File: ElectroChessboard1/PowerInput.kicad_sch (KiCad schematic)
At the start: 8 parts, among them J1 USB_B

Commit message: Added but not connected yet SD Card pins and RTC
.
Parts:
- J1: footprint (none) -> Connector_USB:USB_B_Lumberg_2411_02_Horizontal
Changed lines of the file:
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@@
 			)
 		)
-		(property "Footprint" ""
+		(property "Footprint" "Connector_USB:USB_B_Lumberg_2411_02_Horizontal"
 			(at 48.26 45.72 0)
 			(effects

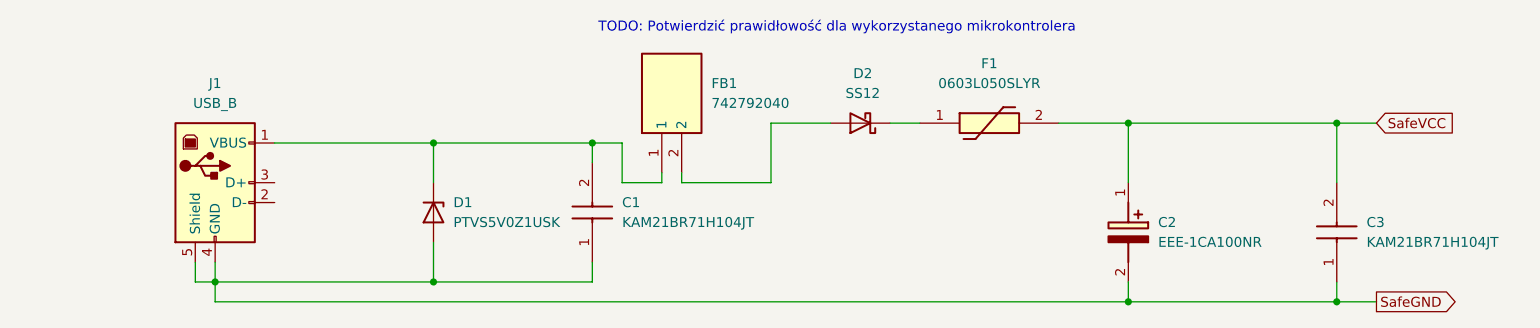
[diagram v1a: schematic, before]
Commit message: Corrected footprints 1
Chosen footprints for JLCPCB
I may add USB insterface chip
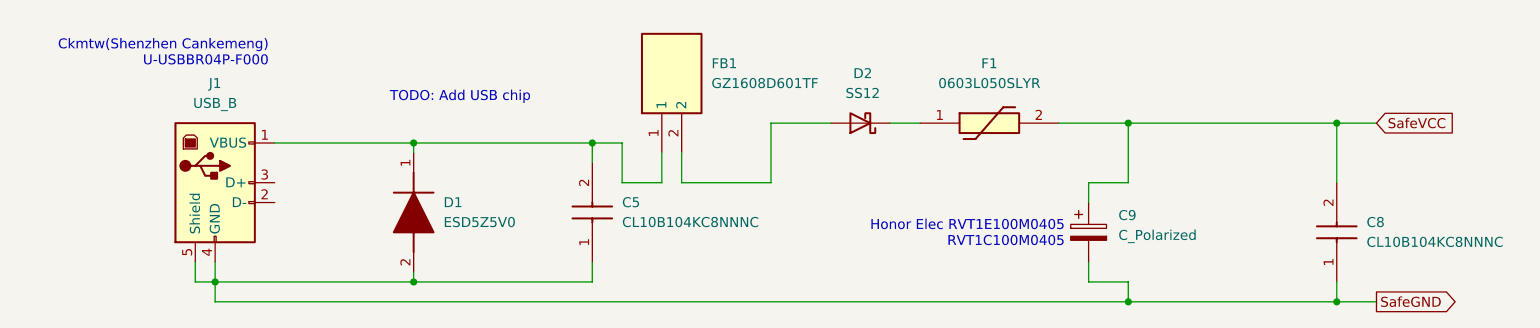
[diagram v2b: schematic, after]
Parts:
- removed C1, C3: KAM21BR71H104JT, CAPC2012X94N, symbol SamacSys_Parts:KAM21BR71H104JT
- removed C2: EEE-1CA100NR, EEE0GA101SR, symbol SamacSys_Parts:EEE-1CA100NR
- removed D1: PTVS5V0Z1USK, Diode_SMD:Nexperia_DSN1608-2_1.6x0.8mm, symbol Diode:PTVS5V0Z1USK
- removed FB1: 742792040, BEADC2012X110N, symbol SamacSys_Parts:742792040
- added C5, C8: CL10B104KC8NNNC, SamacSys_Parts:CAPC1608X90N, symbol SamacSys_Parts:CL10B104KC8NNNC
- added C9: C_Polarized, Capacitor_SMD:CP_Elec_4x5.4, symbol Device:C_Polarized
- added D1: ESD5Z5V0, SODFL1608X70N, symbol SamacSys_Parts:ESD5Z5V0
- added FB1: GZ1608D601TF, BEADC1608X95N, symbol SamacSys_Parts:GZ1608D601TF
- F1: footprint 0603L050SLYR -> SamacSys_Parts:0603L050SLYR
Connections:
- net SafeGND: now also C5.1, C8.1, C9.2, D1.2 (A)
- net SafeVCC: now also C8.2, C9.1
- net at J1.1 (VBUS): now also C5.2, D1.1 (K), FB1.1
- net at D2.2 (A): now also FB1.2
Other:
- note added: "Ckmtw(Shenzhen Cankemeng) U-USBBR04P-F000"
- note added: "Honor Elec RVT1E100M0405 RVT1C100M0405"
- note added: "TODO: Add USB chip"
- note removed: "TODO: Potwierdzić prawidłowość dla wykorzystanego mikrokontrolera"

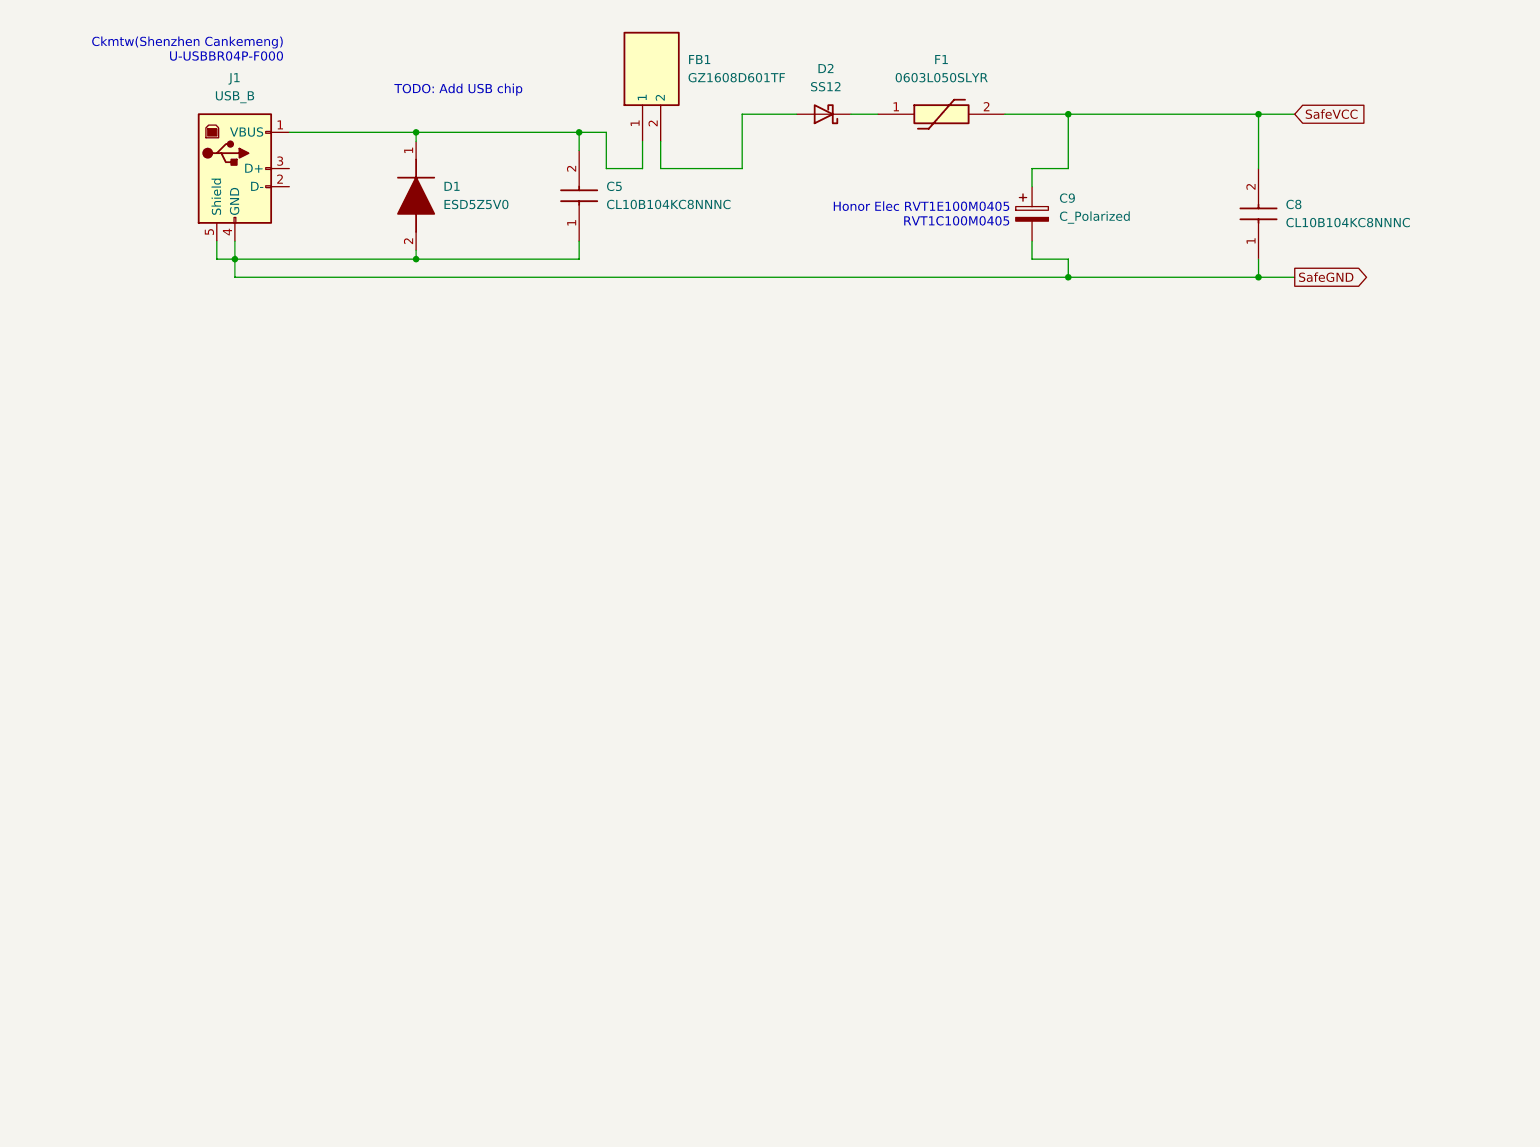
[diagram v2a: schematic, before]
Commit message: Added FT232RL
Ready for PCB design
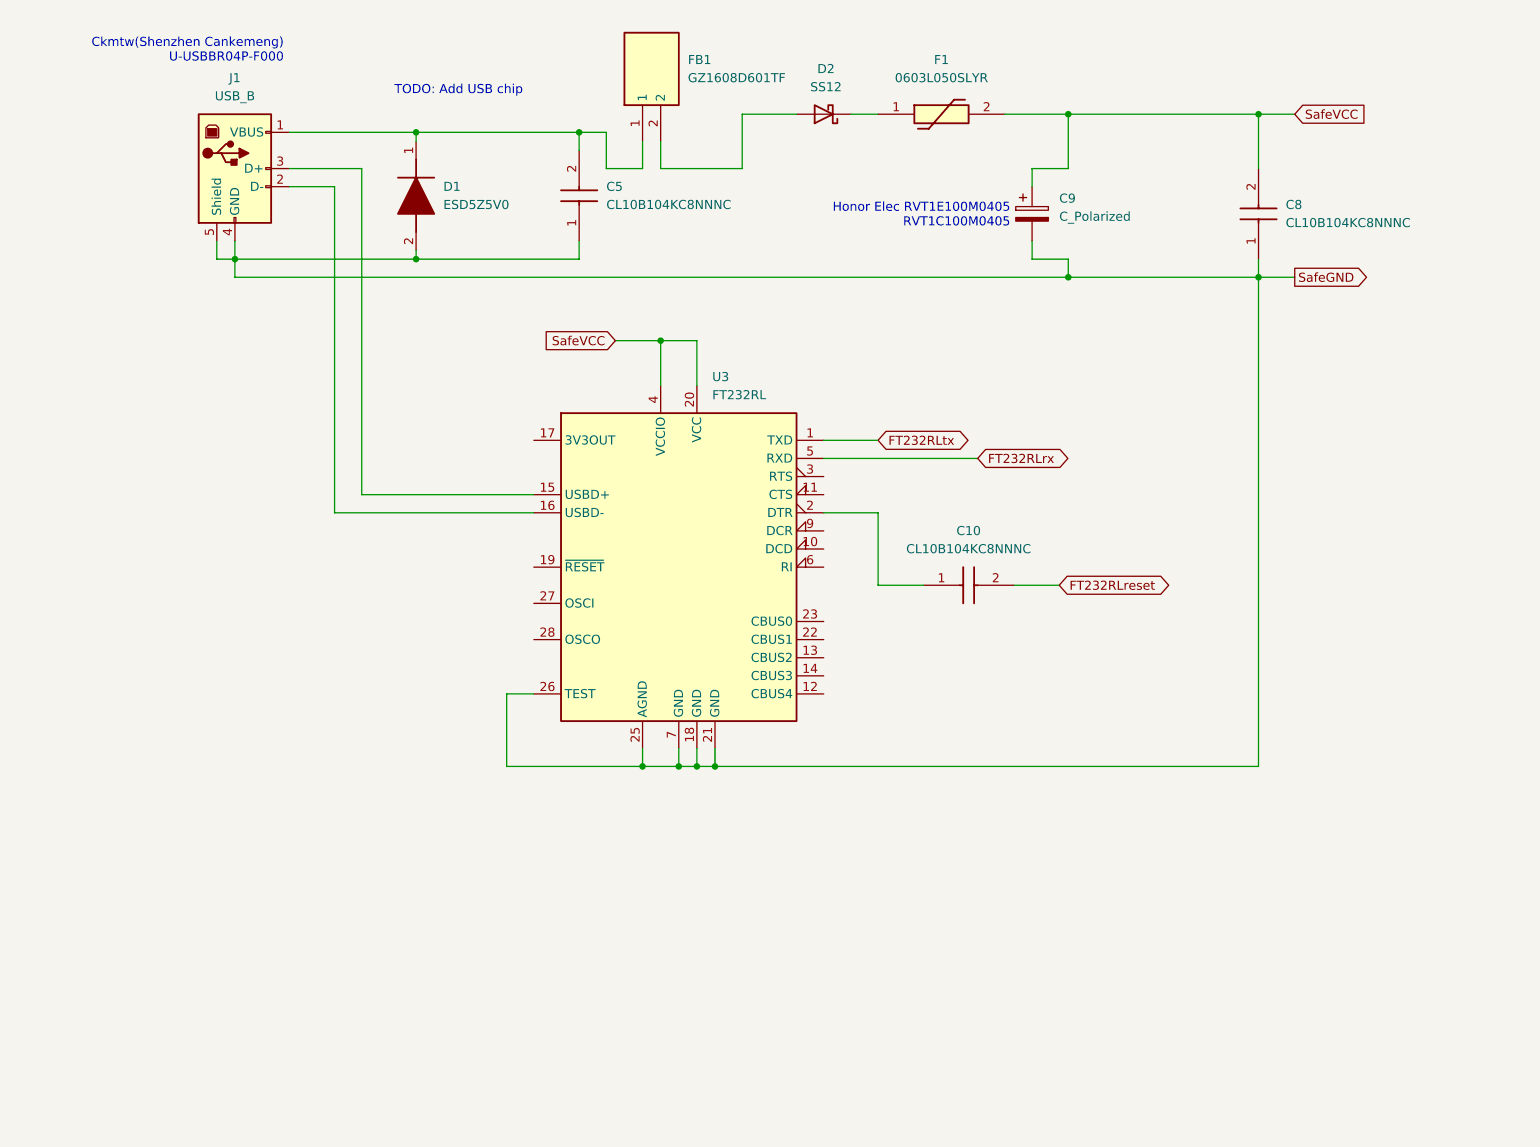
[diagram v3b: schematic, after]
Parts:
- added C10: CL10B104KC8NNNC, SamacSys_Parts:CAPC1608X90N, symbol SamacSys_Parts:CL10B104KC8NNNC
- added U3: FT232RL, Package_SO:SSOP-28_5.3x10.2mm_P0.65mm, symbol Interface_USB:FT232RL
- D1: footprint SODFL1608X70N -> SamacSys_Parts:SODFL1608X70N
- FB1: footprint BEADC1608X95N -> SamacSys_Parts:BEADC1608X95N
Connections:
- net SafeGND: now also U3.18 (GND), U3.21 (GND), U3.25 (AGND), U3.26 (TEST), U3.7 (GND)
- net SafeVCC: now also U3.20 (VCC), U3.4 (VCCIO)
- net at J1.2 (D-): now also U3.16 (USBD-)
- net at J1.3 (D+): now also U3.15 (USBD+)
- new net: C10.1, U3.2 (DTR)
- new net FT232RLreset: C10.2
- new net FT232RLrx: U3.5 (RXD)
- new net FT232RLtx: U3.1 (TXD)

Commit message: USB-C
Changed USB to USB-C and replaced wrong diode, only on schematic
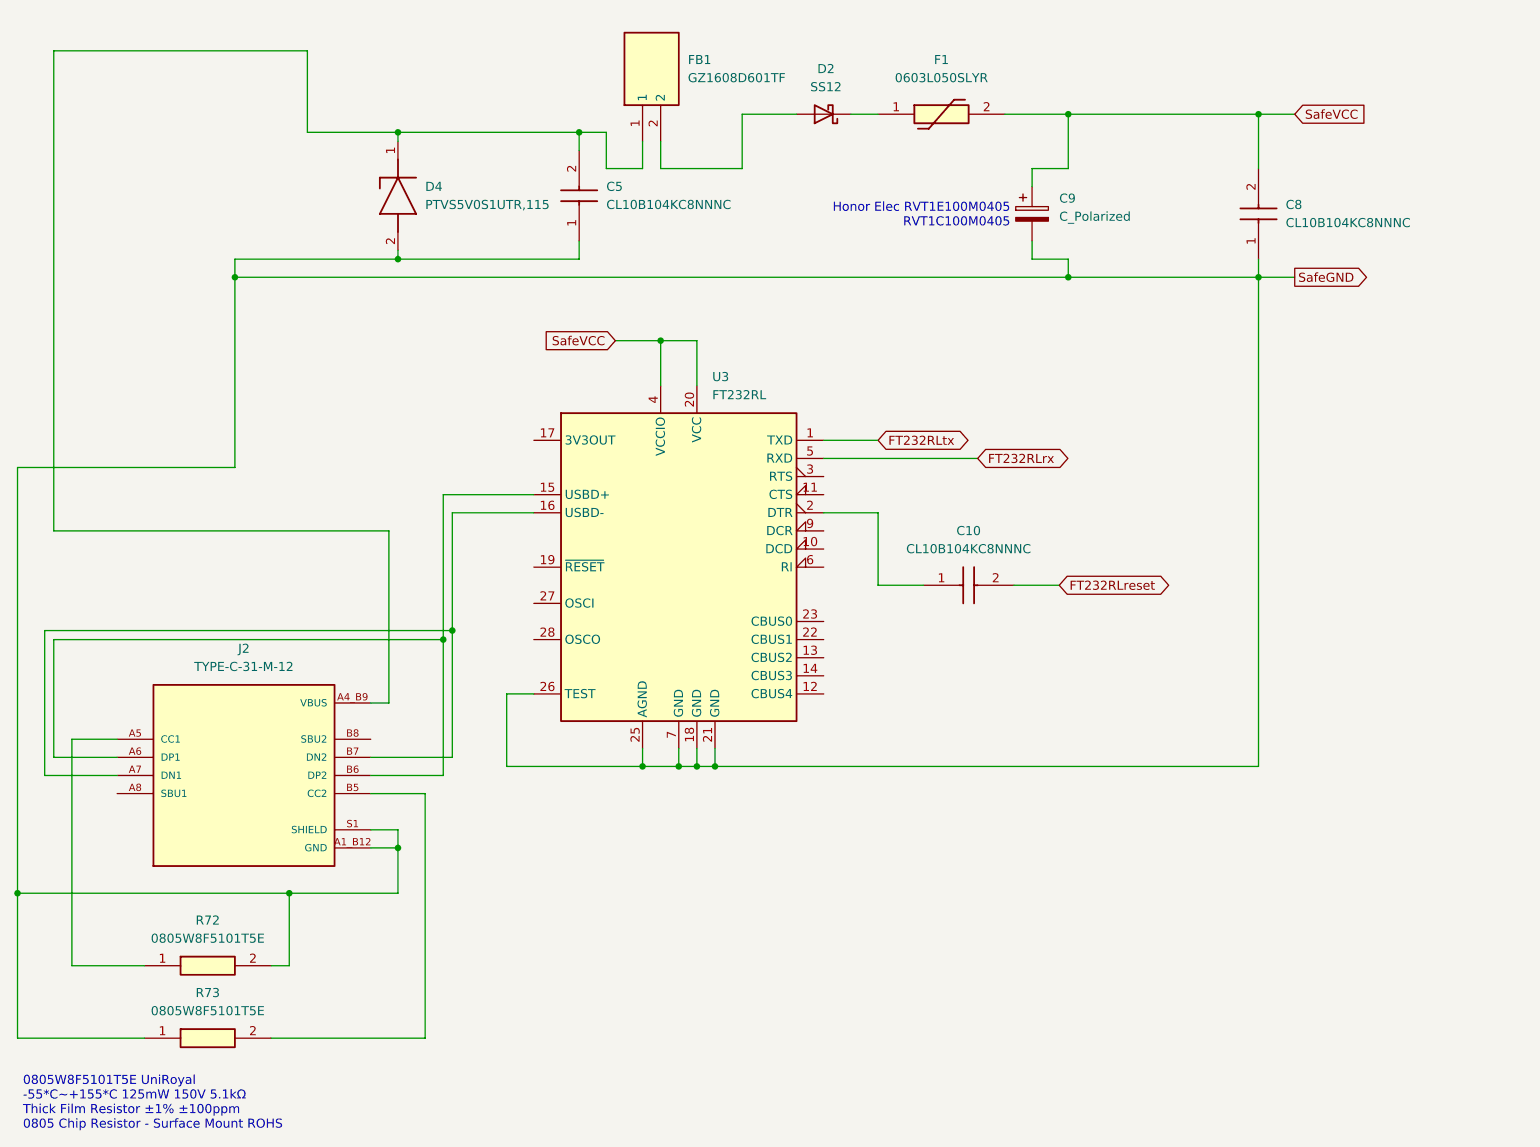
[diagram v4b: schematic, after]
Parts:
- removed D1: ESD5Z5V0, SamacSys_Parts:SODFL1608X70N, symbol SamacSys_Parts:ESD5Z5V0
- removed J1: USB_B, Connector_USB:USB_B_Lumberg_2411_02_Horizontal, symbol Connector:USB_B
- added D4: PTVS5V0S1UTR,115, SOD123W, symbol SamacSys_Parts:PTVS5V0S1UTR,115
- added J2: TYPE-C-31-M-12, TYPE-C-31-M-12:HRO_TYPE-C-31-M-12, symbol TYPE-C-31-M-12:TYPE-C-31-M-12
- added R72, R73: 0805W8F5101T5E, RESC2013X65N, symbol SamacSys_Parts:0805W8F5101T5E
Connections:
- net at U3.15 (USBD+): now also J2.A6 (DP1), J2.B6 (DP2)
- net at U3.16 (USBD-): now also J2.A7 (DN1), J2.B7 (DN2)
- net VBUS: now reaches C5.2, FB1.1
- net VBUS: now also D4.1 (K), J2.A4_B9 (VBUS), J2.B4_A9 (VBUS)
- net SafeGND renamed GND
- net GND: now also D4.2 (A), J2.A1_B12 (GND), J2.B1_A12 (GND), J2.S1 (SHIELD), J2.S2 (SHIELD), J2.S3 (SHIELD), J2.S4 (SHIELD), R72.2, R73.1
- new net: J2.A5 (CC1), R72.1
- new net: J2.B5 (CC2), R73.2
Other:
- note added: "0805W8F5101T5E UniRoyal -55*C~+155*C 125mW 150V 5.1kΩ Thick Film Resistor ±1% ±100ppm 0805 Chip Resistor - Surface Mount ROHS"
- note removed: "Ckmtw(Shenzhen Cankemeng) U-USBBR04P-F000"
- note removed: "TODO: Add USB chip"
